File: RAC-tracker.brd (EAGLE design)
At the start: 31.8 x 50.8 mm, 5 parts

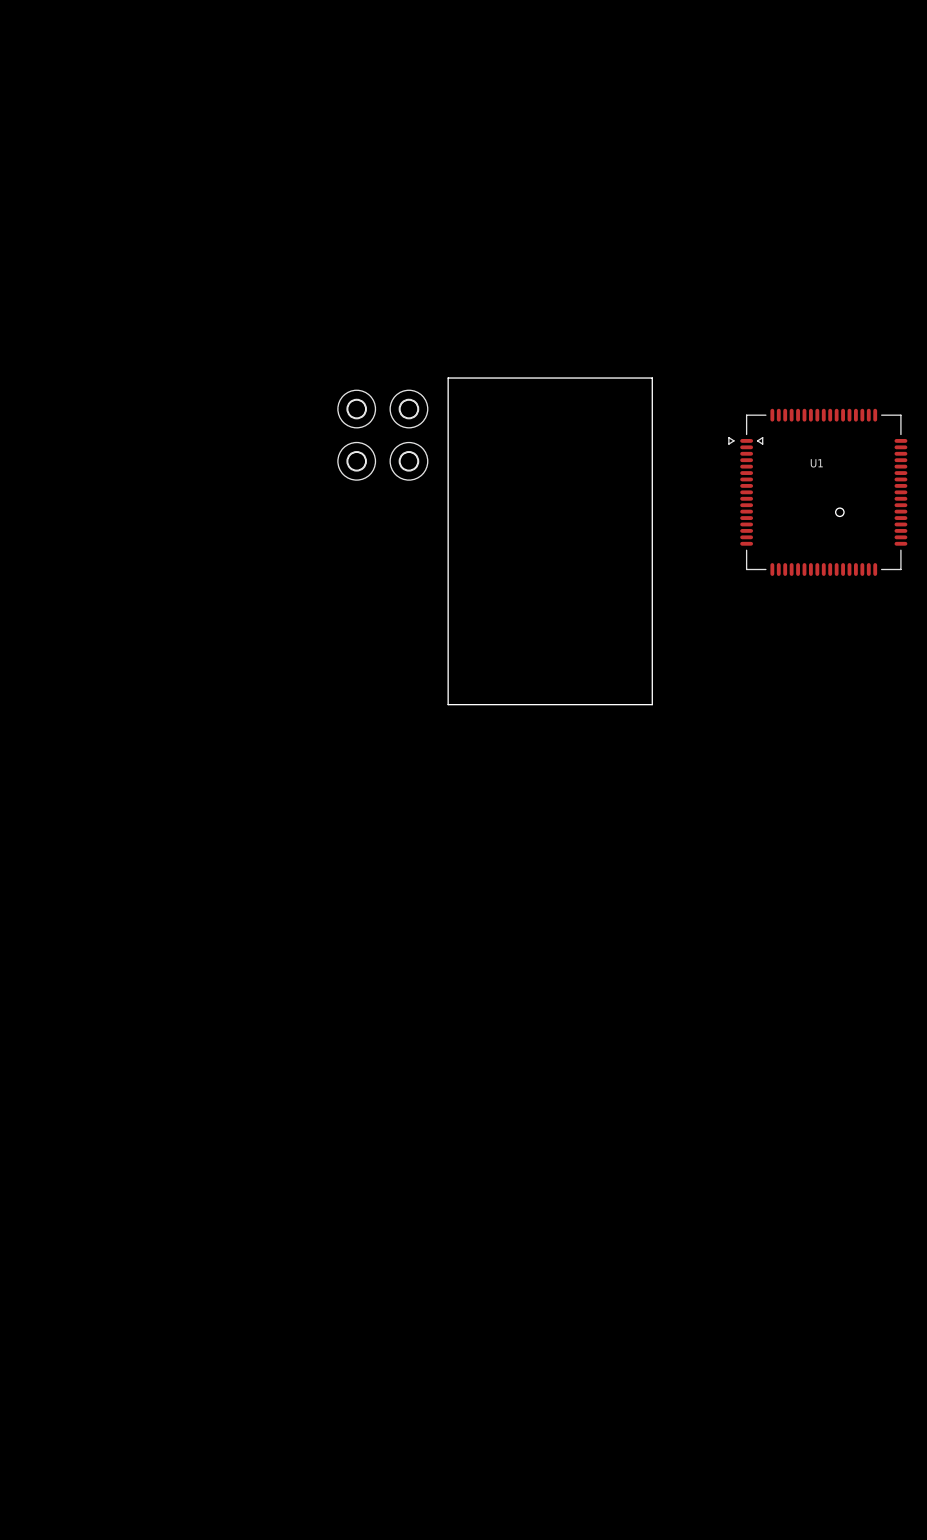
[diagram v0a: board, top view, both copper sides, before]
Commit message: Started connecting the SIM7000
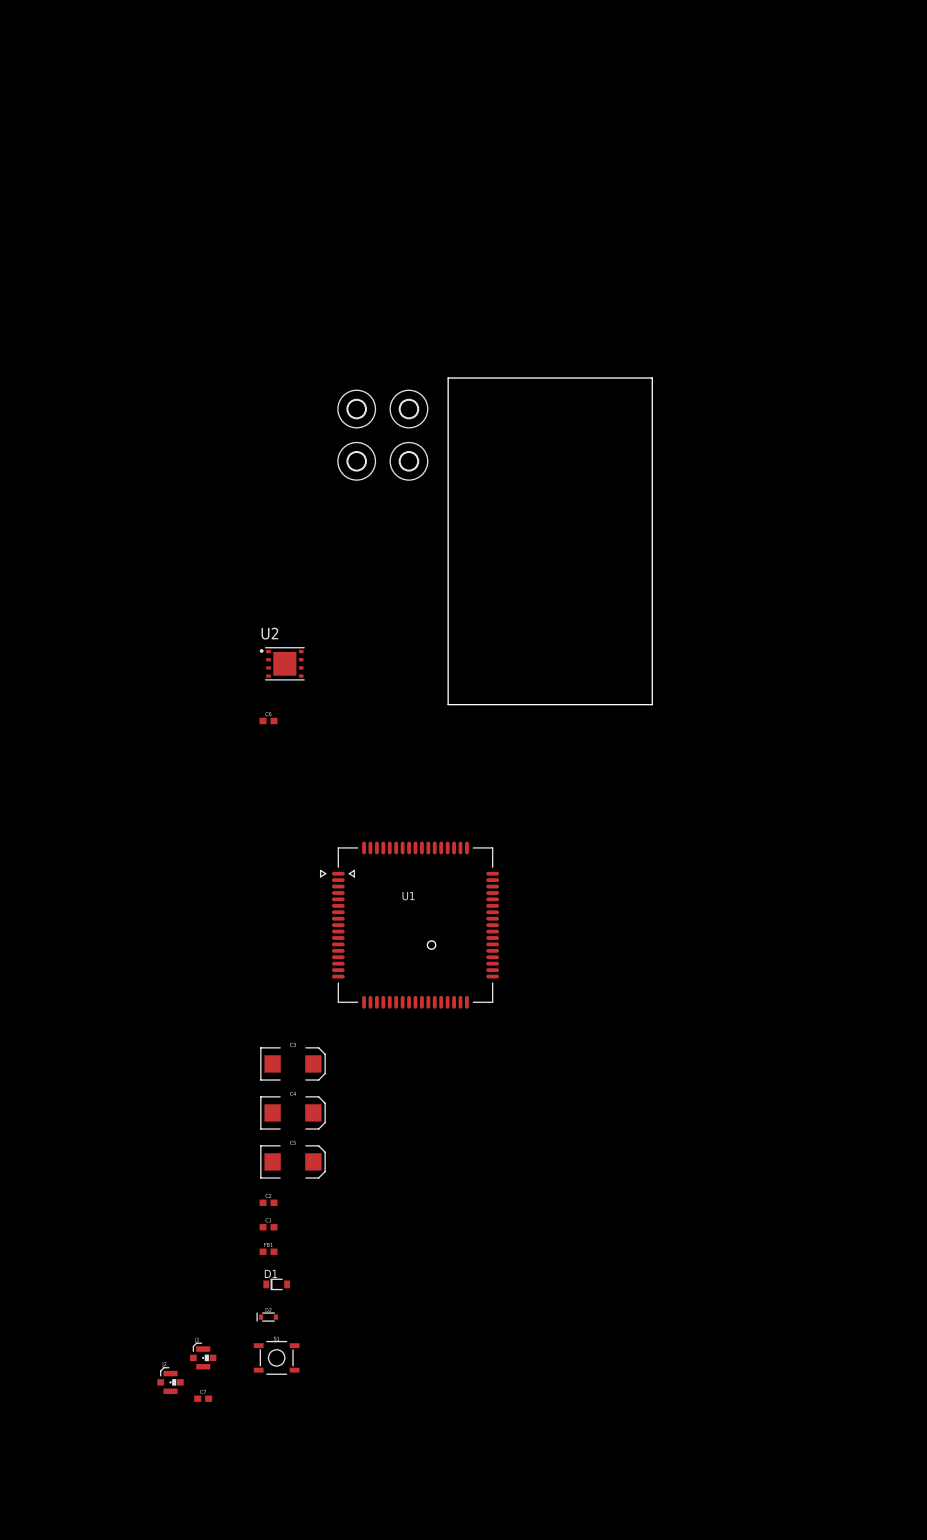
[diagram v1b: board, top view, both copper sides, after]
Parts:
- added C1, C6: 0.1uF, SparkFun-Capacitors:0603
- added C2: 1.0uF, SparkFun-Capacitors:0603
- added C3, C4, C5: 100uF, SparkFun-Capacitors:EIA7343
- added C7: 33pF, SparkFun-Capacitors:0603
- added D1: SMF5.0AT1, diode:SOD123FL
- added D2: 250mA/100V, SparkFun-DiscreteSemi:SOD-323
- added FB1: 30Ω/1.8A, SparkFun-Coils:0603
- added J1, J2: U.FL, SparkFun-Connectors:U.FL
- added S1: MOMENTARY-SWITCH-SPST-SMD-5.2MM, SparkFun-Switches:TACTILE_SWITCH_SMD_5.2MM
- added U2: SIM-ST-MFF2, rocket-components:PSON127P500X600X82-9N
- moved U1 92.5 mm to (-5.08, -34.3)
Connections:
- new net GND: C1.2, C2.2, C3.C, C4.C, C5.C, C6.2, D1.A, J1.1, J1.2, J2.1, J2.2, S1.1, U1.17, U1.18, U1.2, U1.29, U1.39, U1.45, U1.46, U1.54, U1.58, U1.59, U1.61, U1.62, U1.63, U1.64, U1.65, U2.1, U2.9
- new net N$1: J1.FEED, U1.60
- new net N$2: C7.1, U1.53
- new net N$3: C7.2, J2.FEED
- new net PWRKEY: D2.C, S1.3
- new net PWRKEY_AN: D2.A, U1.1
- new net RI: U1.4
- new net RXD: U1.10
- new net SIM_CLK: U1.32, U2.6
- new net SIM_DATA: U1.31, U2.3
- new net SIM_RST: U1.33, U2.7
- new net SIM_VIN: C6.1, U1.30, U2.8
- new net TXD: U1.9
- new net VIN: C1.1, C2.1, C3.A, C4.A, C5.A, FB1.2, U1.55, U1.56, U1.57
- new net V_BATT: D1.C, FB1.1

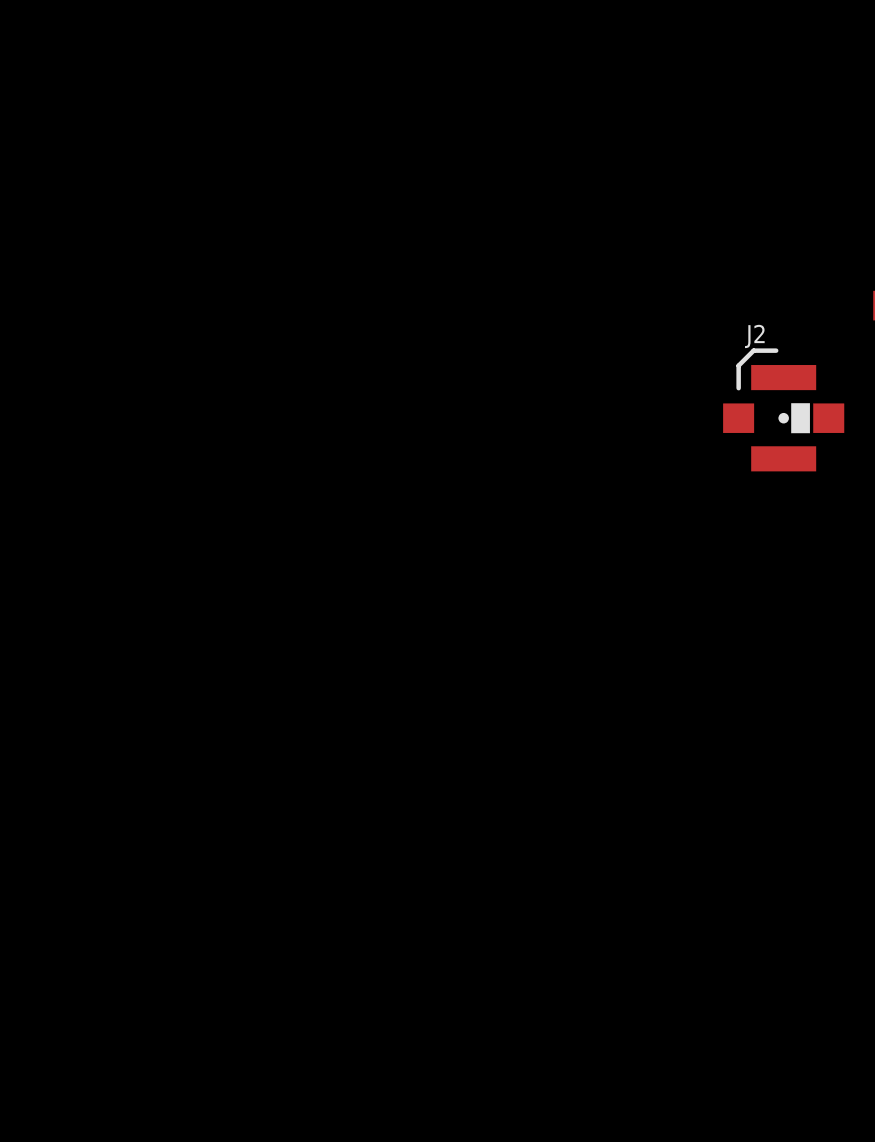
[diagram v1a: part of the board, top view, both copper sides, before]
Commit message: Added LiPo charging circuit, LiPo connector, and USB connector
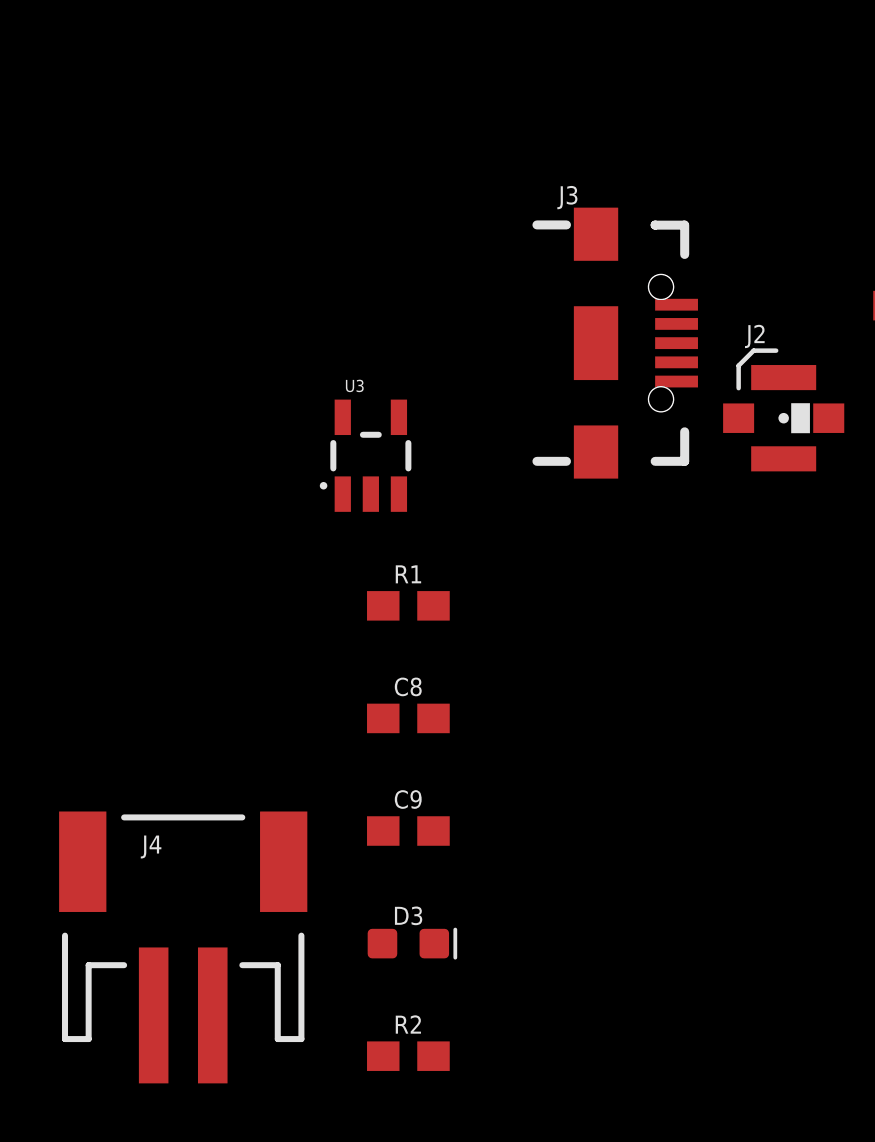
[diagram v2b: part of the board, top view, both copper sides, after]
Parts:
- added C8, C9: 4.7uF, SparkFun-Capacitors:0603
- added D3: RED, SparkFun-LED:LED-0603
- added J3: (no value), SparkFun-Connectors:USB-B-MICRO-SMD
- added J4: (no value), SparkFun-Connectors:JST-2-SMD
- added R1: 2.0k, SparkFun-Resistors:0603
- added R2: 1k, SparkFun-Resistors:0603
- added U3: MCP73831, SparkFun-IC-Power:SOT23-5
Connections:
- new net N$4: R1.2, U3.5
- new net N$5: D3.C, U3.1
- new net N$6: D3.A, R2.1
- new net USB_DM: J3.D-, U1.28
- new net USB_DP: J3.D+, U1.27
- new net V_USB: C8.1, J3.VBUS, R2.2, U1.24, U3.4
- net GND: now also C8.2, C9.2, J3.GND, J3.SHIELD1, J3.SHIELD2, J3.SHIELD3, J4.1, R1.1, U3.2
- net V_BATT: now also C9.1, J4.2, U3.3
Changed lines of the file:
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@@
 <attribute name="VALUE" x="-44.45" y="-107.95" size="0.6096" layer="27" font="vector" ratio="20" align="top-left"/>
+</element>
+<element name="J3" library="SparkFun-Connectors" package="USB-B-MICRO-SMD" value="" x="-49.53" y="-102.87" smashed="yes">
+<attribute name="NAME" x="-50.8" y="-98.171" size="0.6096" layer="25" font="vector" ratio="20"/>
+<attribute name="PROD_ID" value="CONN-11752" x="-49.53" y="-102.87" size="1.778" layer="27" display="off"/>
+<attribute name="VALUE" x="-50.8" y="-107.569" size="0.6096" layer="27" font="vector" ratio="20" align="top-left"/>
+</element>
+<element name="U3" library="SparkFun-IC-Power" package="SOT23-5" value="MCP73831" x="-57.15" y="-106.68" smashed="yes">
+<attribute name="NAME" x="-58.039" y="-104.521" size="0.4064" layer="25"/>
+<attribute name="PROD_ID" value="IC-09995" x="-57.15" y="-106.68" size="1.778" layer="27" display="off"/>
+<attribute name="VALUE" x="-58.1025" y="-106.8705" size="0.4064" layer="27"/>
+</element>
+<element name="R1" library="SparkFun-Resistors" library_urn="urn:adsk.eagle:library:532" package="0603" package3d_urn="urn:adsk.eagle:package:39650/1" value="2.0k" x="-55.88" y="-111.76" smashed="yes">
+<attribute name="NAME" x="-55.88" y="-110.998" size="0.6096" layer="25" font="vector" ratio="20" align="bottom-center"/>
+<attribute name="PROD_ID" value="RES-08296" x="-55.88" y="-111.76" size="1.778" layer="27" display="off"/>
+<attribute name="VALUE" x="-55.88" y="-112.522" size="0.6096" layer="27" font="vector" ratio="20" align="top-center"/>
+</element>
+<element name="C8" library="SparkFun-Capacitors" library_urn="urn:adsk.eagle:library:510" package="0603" package3d_urn="urn:adsk.eagle:package:37414/1" value="4.7uF" x="-55.88" y="-115.57" smashed="yes">
+<attribute name="NAME" x="-55.88" y="-114.808" size="0.6096" layer="25" font="vector" ratio="20" align="bottom-center"/>
+<attribute name="PROD_ID" value="CAP-08280" x="-55.88" y="-115.57" size="1.778" layer="27" display="off"/>
+<attribute name="VALUE" x="-55.88" y="-116.332" size="0.6096" layer="27" font="vector" ratio="20" align="top-center"/>
+</element>
+<element name="C9" library="SparkFun-Capacitors" library_urn="urn:adsk.eagle:library:510" package="0603" package3d_urn="urn:adsk.eagle:package:37414/1" value="4.7uF" x="-55.88" y="-119.38" smashed="yes">
+<attribute name="NAME" x="-55.88" y="-118.618" size="0.6096" layer="25" font="vector" ratio="20" align="bottom-center"/>
+<attribute name="PROD_ID" value="CAP-08280" x="-55.88" y="-119.38" size="1.778" layer="27" display="off"/>
+<attribute name="VALUE" x="-55.88" y="-120.142" size="0.6096" layer="27" font="vector" ratio="20" align="top-center"/>
+</element>
+<element name="D3" library="SparkFun-LED" library_urn="urn:adsk.eagle:library:529" package="LED-0603" package3d_urn="urn:adsk.eagle:package:39354/1" value="RED" x="-55.88" y="-123.19" smashed="yes">
+<attribute name="NAME" x="-55.88" y="-122.555" size="0.6096" layer="25" font="vector" ratio="20" align="bottom-center"/>
+<attribute name="PROD_ID" value="DIO-00819" x="-55.88" y="-123.19" size="1.778" layer="27" display="off"/>
+<attribute name="VALUE" x="-55.88" y="-123.825" size="0.6096" layer="27" font="vector" ratio="20" align="top-center"/>
+</element>
+<element name="R2" library="SparkFun-Resistors" library_urn="urn:adsk.eagle:library:532" package="0603" package3d_urn="urn:adsk.eagle:package:39650/1" value="1k" x="-55.88" y="-127" smashed="yes">
+<attribute name="NAME" x="-55.88" y="-126.238" size="0.6096" layer="25" font="vector" ratio="20" align="bottom-center"/>
+<attribute name="PROD_ID" value="RES-07856" x="-55.88" y="-127" size="1.778" layer="27" display="off"/>
+<attribute name="VALUE" x="-55.88" y="-127.762" size="0.6096" layer="27" font="vector" ratio="20" align="top-center"/>
+</element>
+<element name="J4" library="SparkFun-Connectors" package="JST-2-SMD" value="" x="-63.5" y="-121.92" smashed="yes">
+<attribute name="NAME" x="-64.897" y="-120.142" size="0.6096" layer="25" font="vector" ratio="20"/>
+<attribute name="PROD_ID" value="CONN-11443" x="-63.5" y="-121.92" size="1.778" layer="27" display="off"/>
+<attribute name="SF_ID" value="PRT-08612" x="-63.5" y="-121.92" size="1.778" layer="27" display="off"/>
+<attribute name="VALUE" x="-65.151" y="-121.285" size="0.6096" layer="27" font="vector" ratio="20"/>
 </element>
 </elements>
@@
 <contactref element="J2" pad="2"/>
 <contactref element="J2" pad="1"/>
-<wire x1="-43.18" y1="-104.035" x2="-43.18" y2="-106.785" width="0" layer="19" extent="1-1"/>
+<contactref element="J3" pad="SHIELD1"/>
+<contactref element="J3" pad="SHIELD2"/>
+<contactref element="J3" pad="SHIELD3"/>
+<contactref element="J3" pad="GND"/>
+<contactref element="R1" pad="1"/>
+<contactref element="C9" pad="2"/>
+<contactref element="U3" pad="2"/>
+<contactref element="C8" pad="2"/>
+<contactref element="J4" pad="1"/>
+<wire x1="-55.03" y1="-119.38" x2="-64.5" y2="-125.62" width="0" layer="19" extent="1-1"/>
+<wire x1="-55.03" y1="-115.57" x2="-55.03" y2="-119.38" width="0" layer="19" extent="1-1"/>
+<wire x1="-56.73" y1="-111.76" x2="-55.03" y2="-115.57" width="0" layer="19" extent="1-1"/>
+<wire x1="-57.15" y1="-107.9801" x2="-56.73" y2="-111.76" width="0" layer="19" extent="1-1"/>
+<wire x1="-49.53" y1="-106.555" x2="-57.15" y2="-107.9801" width="0" layer="19" extent="1-1"/>
+<wire x1="-46.805" y1="-104.17" x2="-49.53" y2="-106.555" width="0" layer="19" extent="1-1"/>
+<wire x1="-49.53" y1="-102.87" x2="-46.805" y2="-104.17" width="0" layer="19" extent="1-1"/>
+<wire x1="-43.18" y1="-104.035" x2="-46.805" y2="-104.17" width="0" layer="19" extent="1-1"/>
+<wire x1="-43.18" y1="-106.785" x2="-43.18" y2="-104.035" width="0" layer="19" extent="1-1"/>
+<wire x1="-49.53" y1="-99.185" x2="-49.53" y2="-102.87" width="0" layer="19" extent="1-1"/>
 <wire x1="-38.1" y1="-102.975" x2="-43.18" y2="-104.035" width="0" layer="19" extent="1-1"/>
 <wire x1="-38.1" y1="-100.225" x2="-38.1" y2="-102.975" width="0" layer="19" extent="1-1"/>
@@
 <contactref element="D1" pad="C"/>
 <contactref element="FB1" pad="1"/>
+<contactref element="U3" pad="3"/>
+<contactref element="C9" pad="1"/>
+<contactref element="J4" pad="2"/>
+<wire x1="-56.73" y1="-119.38" x2="-62.5" y2="-125.62" width="0" layer="19" extent="1-1"/>
+<wire x1="-56.2" y1="-107.9801" x2="-56.73" y2="-119.38" width="0" layer="19" extent="1-1"/>
+<wire x1="-28.295" y1="-90.17" x2="-56.2" y2="-107.9801" width="0" layer="19" extent="1-1"/>
 <wire x1="-28.79" y1="-85.09" x2="-28.295" y2="-90.17" width="0" layer="19" extent="1-1"/>
 </signal>
@@
 <wire x1="-37.25" y1="-107.95" x2="-41.655" y2="-105.41" width="0" layer="19" extent="1-1"/>
 </signal>
+<signal name="V_USB">
+<contactref element="J3" pad="VBUS"/>
+<contactref element="U1" pad="24"/>
+<contactref element="R2" pad="2"/>
+<contactref element="U3" pad="4"/>
+<contactref element="C8" pad="1"/>
+<wire x1="-56.73" y1="-115.57" x2="-55.03" y2="-127" width="0" layer="19" extent="1-1"/>
+<wire x1="-56.2" y1="-105.3799" x2="-56.73" y2="-115.57" width="0" layer="19" extent="1-1"/>
+<wire x1="-46.805" y1="-101.57" x2="-56.2" y2="-105.3799" width="0" layer="19" extent="1-1"/>
+<wire x1="-7.08" y1="-46.29" x2="-46.805" y2="-101.57" width="0" layer="19" extent="1-1"/>
+</signal>
+<signal name="USB_DM">
+<contactref element="U1" pad="28"/>
+<contactref element="J3" pad="D-"/>
+<wire x1="-3.08" y1="-46.29" x2="-46.805" y2="-102.22" width="0" layer="19" extent="1-1"/>
+</signal>
+<signal name="USB_DP">
+<contactref element="U1" pad="27"/>
+<contactref element="J3" pad="D+"/>
+<wire x1="-4.08" y1="-46.29" x2="-46.805" y2="-102.87" width="0" layer="19" extent="1-1"/>
+</signal>
+<signal name="N$4">
+<contactref element="U3" pad="5"/>
+<contactref element="R1" pad="2"/>
+<wire x1="-58.1" y1="-105.3799" x2="-55.03" y2="-111.76" width="0" layer="19" extent="1-1"/>
+</signal>
+<signal name="N$5">
+<contactref element="D3" pad="C"/>
+<contactref element="U3" pad="1"/>
+<wire x1="-58.1" y1="-107.9801" x2="-55.003" y2="-123.19" width="0" layer="19" extent="1-1"/>
+</signal>
+<signal name="N$6">
+<contactref element="D3" pad="A"/>
+<contactref element="R2" pad="1"/>
+<wire x1="-56.757" y1="-123.19" x2="-56.73" y2="-127" width="0" layer="19" extent="1-1"/>
+</signal>
 </signals>

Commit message: Renamed nets and started board placement
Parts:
- moved J2 220.5 mm to (25.4, 104.1)
- moved C7 217.7 mm to (25.4, 100.3)
- moved J1 210.0 mm to (3.81, 104.1)
- moved R2 176.6 mm to (-17.8, 45.5), turned to 180 degrees
- moved C9 173.8 mm to (-14.4, 49.4), turned to 270 degrees
- moved D3 171.2 mm to (-17.8, 43.7)
- moved C8 169.4 mm to (-21.0, 50.2), turned to 90 degrees
- moved C3 168.0 mm to (67.3, 85.1)
- moved C4 168.0 mm to (67.3, 77.5)
- moved C5 168.0 mm to (67.3, 69.8)
- moved D1 168.0 mm to (64.8, 50.8)
- moved D2 168.0 mm to (63.5, 45.7)
- moved FB1 168.0 mm to (63.5, 55.9)
- moved S1 168.0 mm to (64.8, 39.4)
- moved C1 162.2 mm to (19.7, 73.8), turned to 180 degrees
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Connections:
- net N$1 renamed LTE_OUT
- net N$2 renamed GNSS_RF
- net N$3 renamed GNSS_OUT
- net N$4 renamed PROG
- net N$5 renamed STAT
- net N$6 renamed STAT_AN
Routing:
- net GND: track 0.00 -> 15.2 mm, vias 0 -> 4
- net V_USB: track 0.00 -> 7.28 mm
- net STAT: track 0.00 -> 6.15 mm
- net SIM_VIN: track 0.00 -> 3.23 mm
- net V_BATT: track 0.00 -> 2.86 mm
- net STAT_AN: track 0.00 -> 2.49 mm
- net PROG: track 0.00 -> 1.92 mm
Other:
- board size 31.8 x 50.8 mm -> 31.8 x 97.8 mm

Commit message: Added GPS frontend, further integrated NRF9160
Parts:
- added C10, C11: 4.7uF, SparkFun-Capacitors:0603
- added C12: 1nF, SparkFun-Capacitors:0603
- added J5, J6: U.FL, SparkFun-Connectors:U.FL
- added L1: 10nH, rocket-components:INDC1608X100N
- added R3: 10k, SparkFun-Resistors:0603
- added R4: 1M, SparkFun-Resistors:0603
- added U4: NRF9160-SICA-R, rocket-components:NORDIC_NRF9160-SICA-R
- added U5: (no value), rocket-components:HFFP10-CD
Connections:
- new net 3.3V: C11.1, C12.1, U4.12, U5.3
- new net GPS_ANT: J5.FEED, U5.5
- new net GPS_EN: R4.2, U4.55, U5.2
- new net GPS_RF: U4.67, U5.10
- new net IO_SUPPLY: U4.13
- new net N$1: R3.1, U4.101
- new net N$2: J6.FEED, U4.61
- new net N$3: L1.2, U5.7
- new net N$4: L1.1, U5.8
- new net VIO: U4.57
- net GND: now also C10.2, C11.2, C12.2, J5.1, J5.2, J6.1, J6.2, R4.1, U4.1, U4.103_1, U4.103_10, U4.103_11, U4.103_12, U4.103_13, U4.103_14, U4.103_15, U4.103_16, U4.103_17, U4.103_18, U4.103_19, U4.103_2, U4.103_20, U4.103_21, U4.103_22, U4.103_23, U4.103_24, U4.103_25, U4.103_26, U4.103_27, U4.103_28, U4.103_29, U4.103_3, U4.103_30, U4.103_31, U4.103_32, U4.103_33, U4.103_34, U4.103_35, U4.103_4, U4.103_5, U4.103_6, U4.103_7, U4.103_8, U4.103_9, U4.14, U4.17, U4.21, U4.27, U4.31, U4.36, U4.41, U4.44, U4.47, U4.5, U4.50, U4.52, U4.56, U4.60, U4.62, U4.63, U4.65, U4.66, U4.72, U4.74, U4.75, U4.76, U4.77, U4.78, U4.79, U4.80, U4.81, U4.82, U4.85, U4.9, U4.90, U4.94, U4.98, U5.1, U5.4, U5.6, U5.9, U5.EP
- net SIM_CLK: now also U4.46
- net SIM_DATA: now also U4.48
- net SIM_RST: now also U4.43
- net SIM_VIN: now also U4.49
- net V_BATT: now also C10.1, R3.2, U4.102, U4.22
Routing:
- net GND: track 15.2 -> 0.00 mm, vias 4 -> 0
- net V_USB: track 7.28 -> 0.00 mm
- net STAT: track 6.15 -> 0.00 mm
- net SIM_VIN: track 3.23 -> 0.00 mm
- net V_BATT: track 2.86 -> 0.00 mm
- net STAT_AN: track 2.49 -> 0.00 mm
- net PROG: track 1.92 -> 0.00 mm
